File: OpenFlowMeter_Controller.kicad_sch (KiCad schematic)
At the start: 37 parts, among them J3 Conn_01x06, J5 Conn_01x03, J6 Conn_02x04_Odd_Even, J7 Conn_02x03_Odd_Even, U2 STM32F103C8Tx, U5 SN65HVD231, U7 24LC64, Y1 12 MHz

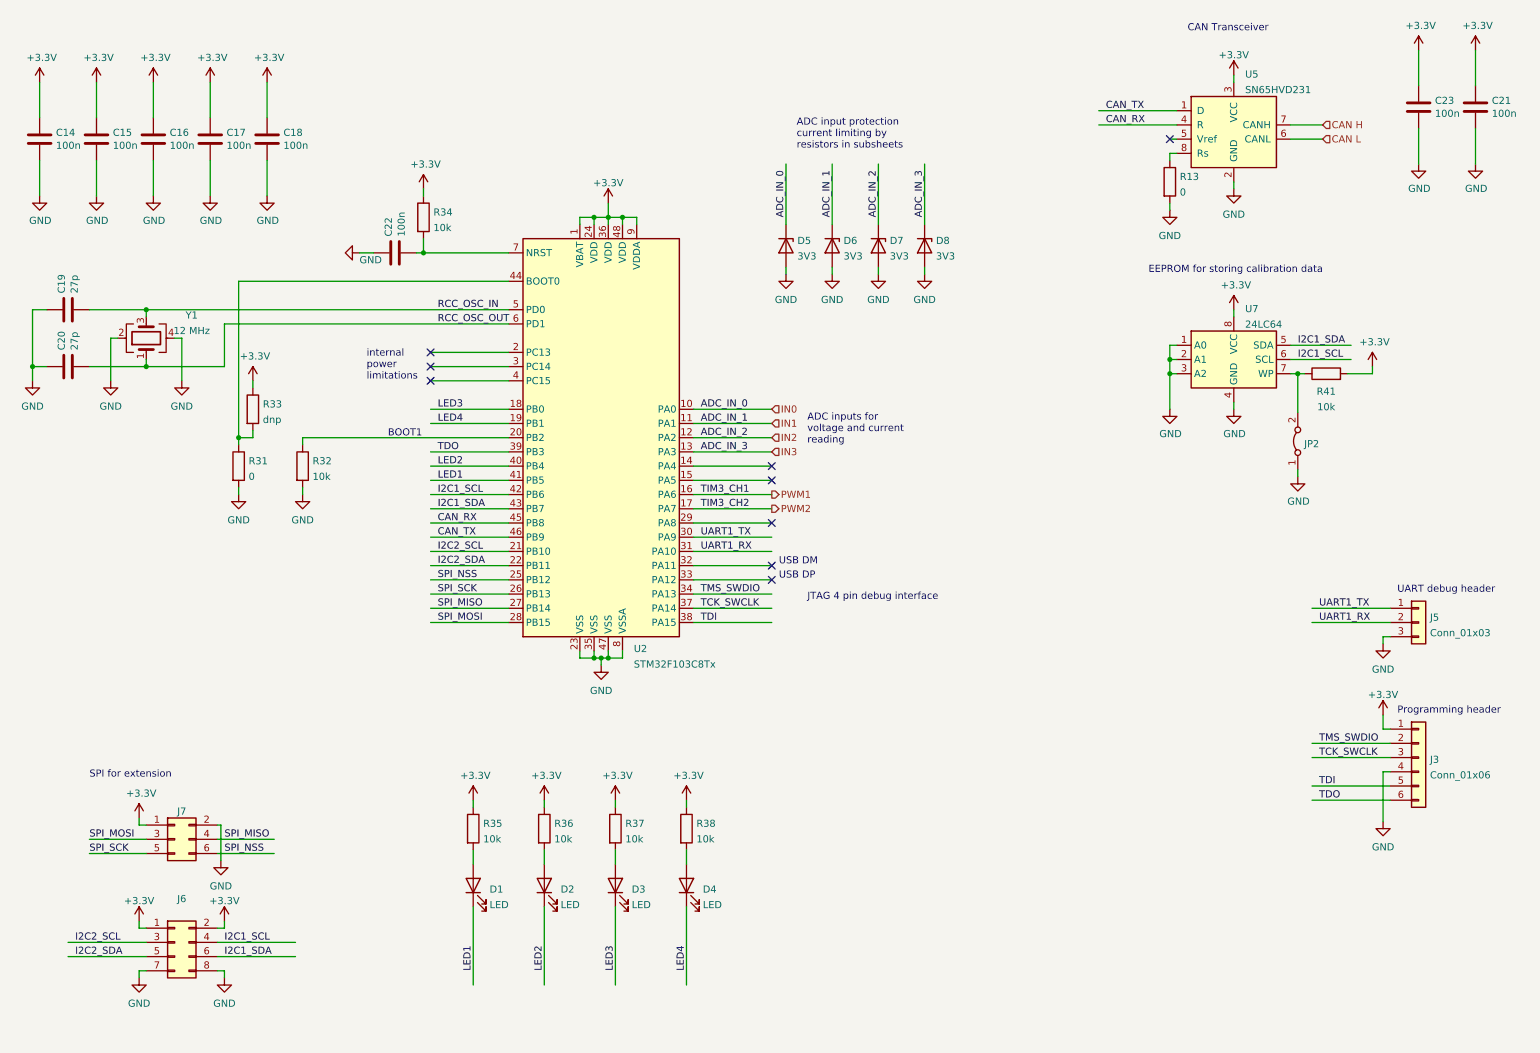
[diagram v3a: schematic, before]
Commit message: added some annotations to the schematic
put labels around functional blocks
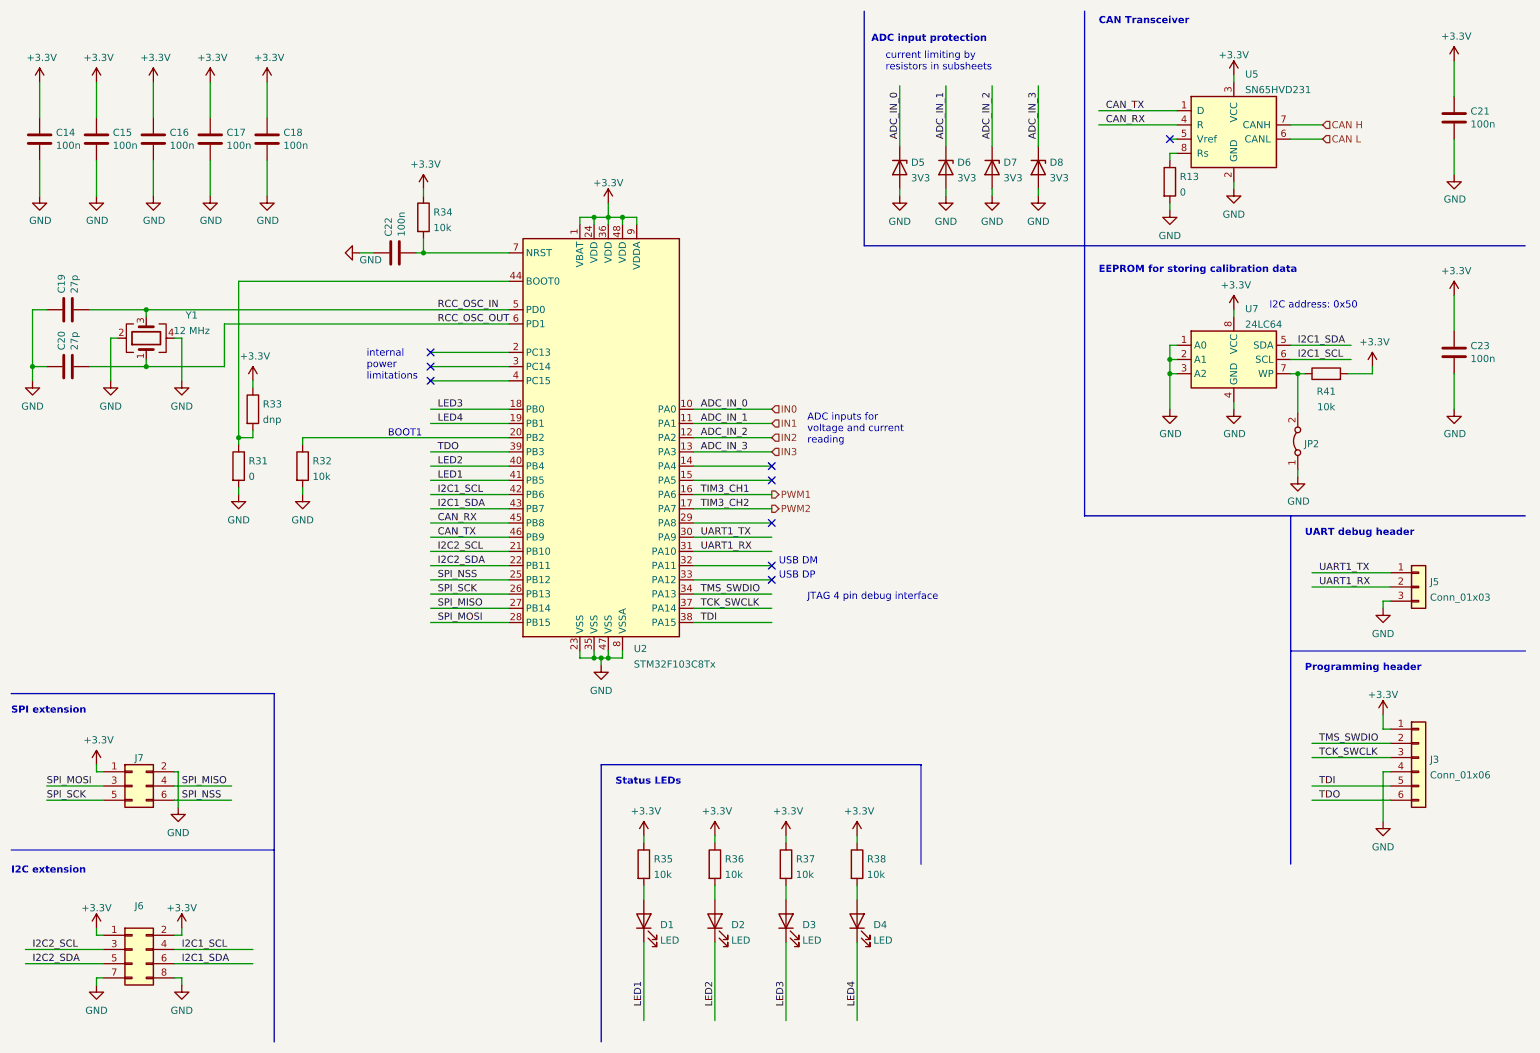
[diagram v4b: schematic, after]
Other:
- note added: "ADC input protection"
- note added: "I2C address: 0x50"
- note added: "I2C extension"
- note added: "SPI extension"
- note added: "Status LEDs"
- note added: "current limiting by resistors in subsheets"
- note removed: "ADC input protection current limiting by resistors in subsheets"
- note removed: "SPI for extension"
- moved on the sheet: C21, C23, D1, D2, D3, D4, D5, D6, D7, D8, J5, J6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

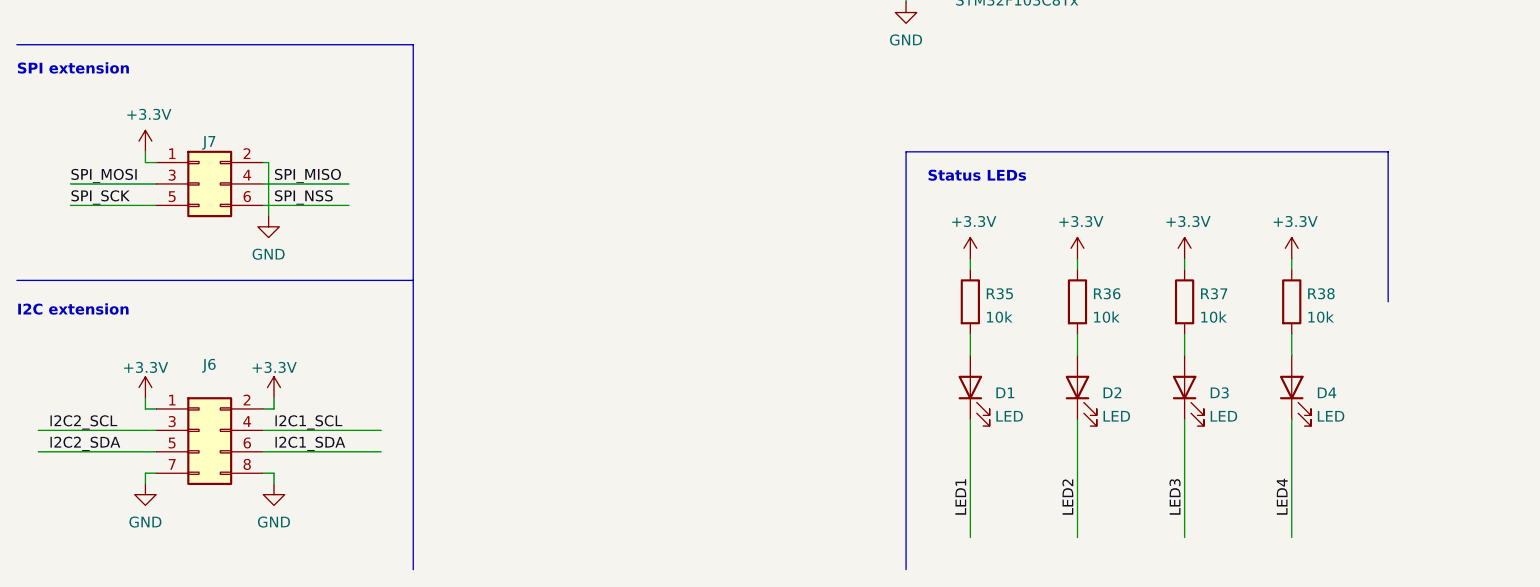
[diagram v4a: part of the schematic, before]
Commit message: added I2C pullups
previous version I have forgotten to add the I2C pullup resistors. Implemented them and added them to the layout.
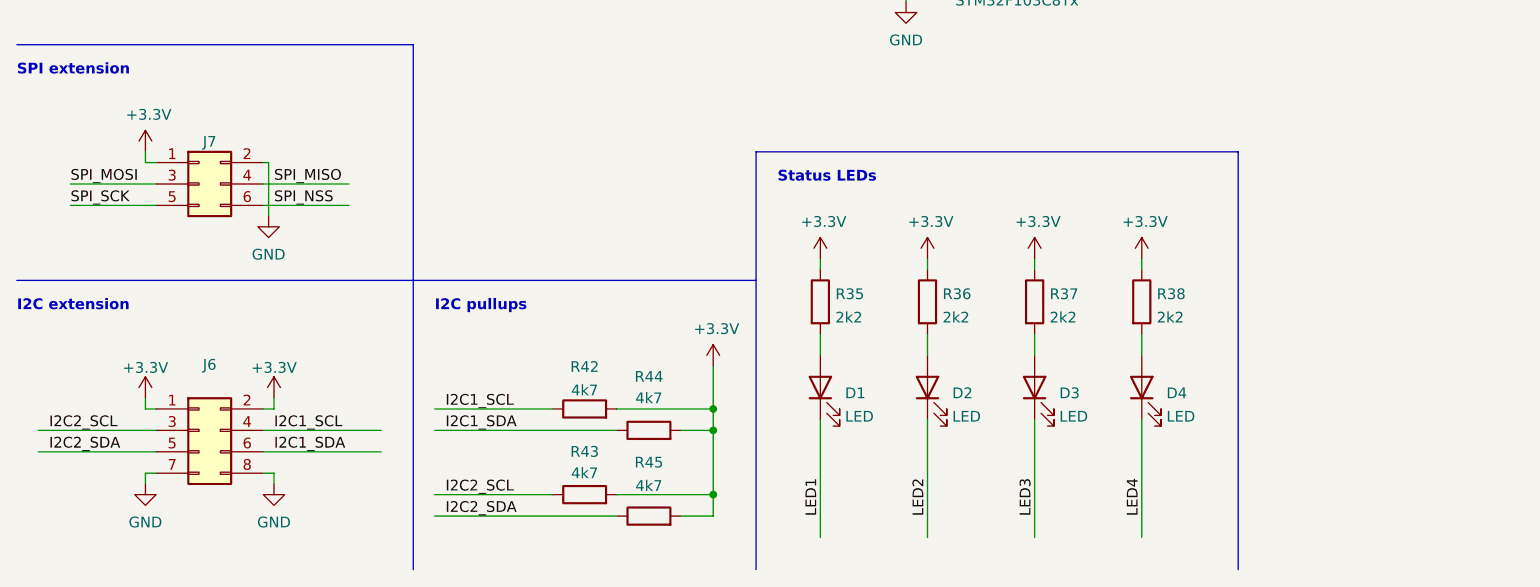
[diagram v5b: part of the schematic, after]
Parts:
- added R42, R43, R44, R45: 4k7, Resistor_SMD:R_0603_1608Metric, symbol Device:R
- R35, R36, R37, R38: value 10k -> 2k2
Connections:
- net +3V3: now also R42.2, R43.2, R44.2, R45.2
- net I2C1_SCL: now also R42.1
- net I2C1_SDA: now also R44.1
- net I2C2_SCL: now also R43.1
- net I2C2_SDA: now also R45.1
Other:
- note added: "I2C pullups"
- moved on the sheet: D1, D2, D3, D4, R35, R36, R37, R38

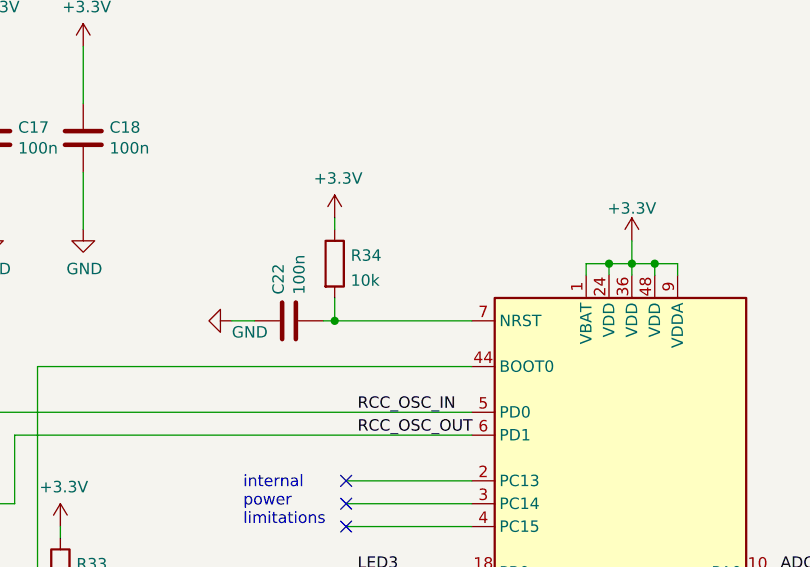
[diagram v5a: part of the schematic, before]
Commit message: added comment of placed resistor value
Because I had a temporary shortage on 10k resistors, I used 8k2 here.
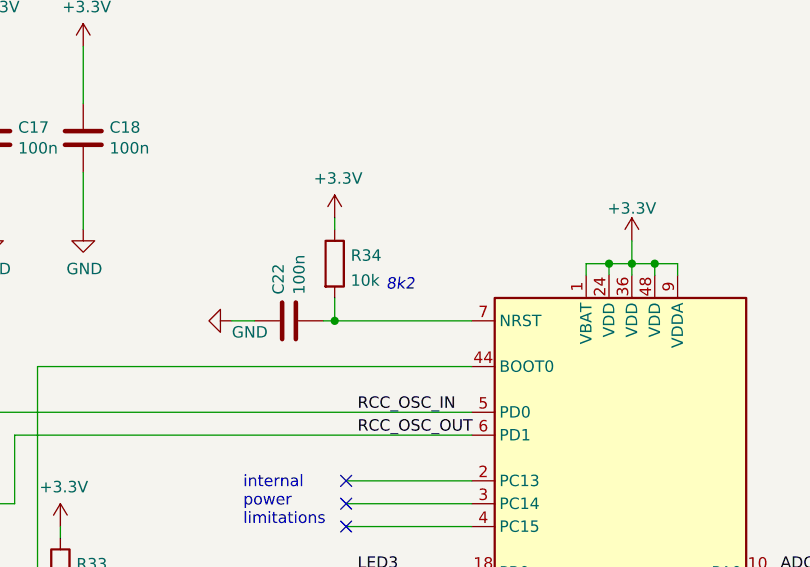
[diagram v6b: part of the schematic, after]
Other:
- note added: "8k2"
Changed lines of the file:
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@@
     (effects (font (size 1.27 1.27)) (justify left bottom))
+  )
+  (text "8k2" (at 93.345 52.705 0)
+    (effects (font (size 1.27 1.27) italic) (justify left bottom))
   )
   (text "I2C extension" (at 13.97 166.37 0)

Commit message: added comments
added some comments to resistors
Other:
- note added: "Not on board v1.0"
- note added: "With 2k2 the LEDs are quite dimmed. Maybe reduce to 1k2."
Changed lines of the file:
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@@
     (stroke (width 0) (type default) (color 0 0 0 0))
+  )
+  (text "With 2k2 the LEDs are quite dimmed.\nMaybe reduce to 1k2."
+    (at 159.385 152.4 0)
+    (effects (font (size 1.27 1.27) italic) (justify left bottom))
   )
   (text "JTAG 4 pin debug interface" (at 156.21 118.11 0)
@@
     (effects (font (size 1.27 1.27) italic) (justify left bottom))
   )
+  (text "Not on board v1.0" (at 71.12 161.925 0)
+    (effects (font (size 1.27 1.27)) (justify left bottom))
+  )
   (text "I2C extension" (at 13.97 166.37 0)

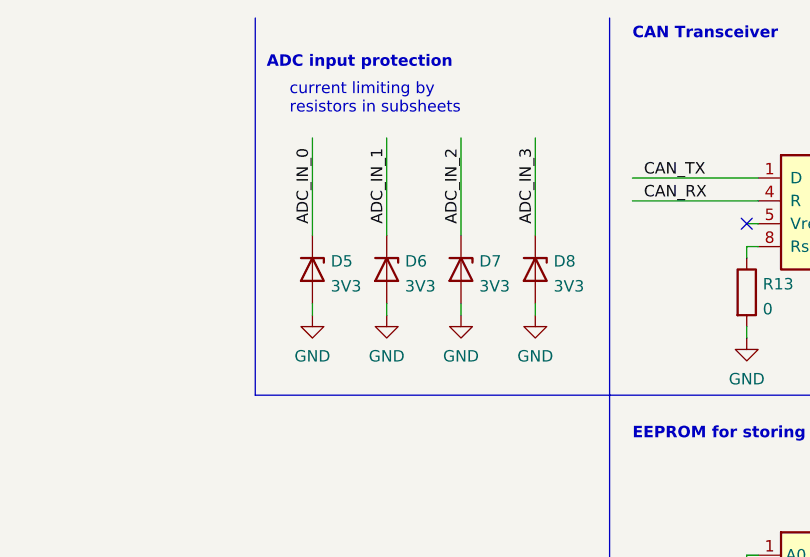
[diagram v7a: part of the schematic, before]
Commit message: implemented changes from tests with the prototype
schematic is updated, layout needs to be done.
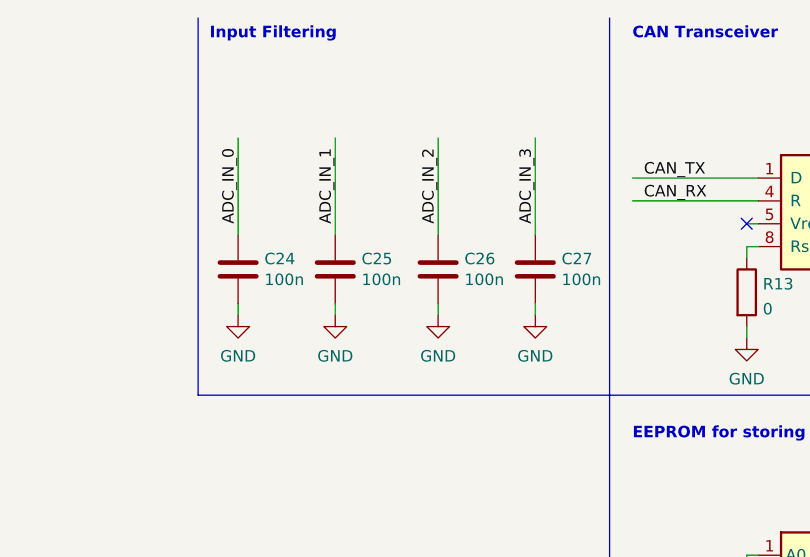
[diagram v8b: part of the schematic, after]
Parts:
- removed D5, D6, D7, D8: 3V3, Diode_SMD:D_MiniMELF, symbol Device:D_Zener
- added C24, C25, C26, C27: 100n, Capacitor_SMD:C_0603_1608Metric, symbol Device:C
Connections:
- net GND: now also C24.2, C25.2, C26.2, C27.2
- net IN0: now also C24.1
- net IN1: now also C25.1
- net IN2: now also C26.1
- net IN3: now also C27.1
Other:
- note added: "Input Filtering"
- note removed: "ADC input protection"
- note removed: "current limiting by resistors in subsheets"
